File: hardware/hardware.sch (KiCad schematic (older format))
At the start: 76 parts, among them J1 DB25_Female, J2 USB_B_Micro, J3 RJ45_Bel_SI-60062-F-68net, J4 Conn_02x06_Odd_Even, U1 LD1117S33TR_SOT223, U11 ENC28J60x-SO, U12 74HC14, U2 74LS126, U3 74LS126, U4 LM1117-ADJ, U5 74LS126, U6 74LS126, U7 STM32F072R8Tx, U8 74LS245, Y1 8MHz, Y2 25MHz

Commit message: feat: split 15 resistor array into single resistors
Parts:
- removed R8: resistor_array_15, Package_SO:SOIC-16_3.9x9.9mm_P1.27mm, symbol 68net:resistor_array_15
- added R21, R22, R23, R24, R25, R26, R27, R28, R29, R30, R31, R32, R33, R34, R8: 3k3, Resistor_SMD:R_0805_2012Metric_Pad1.15x1.40mm_HandSolder, symbol Device:R
- J4: footprint Connector_PinHeader_1.27mm:PinHeader_2x06_P1.27mm_Vertical -> Connector_PinSocket_2.54mm:PinSocket_2x06_P2.54mm_Vertical
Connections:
- wire segments 531 -> 559
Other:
- note added: "Extension port"
- note removed: "Expansion port"
- moved on the sheet: U2A, U2B, U2C, U2D, U3A, U3C, U3D, U5A, U5B, U5C, U5D, U6A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

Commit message: feat: finalize revA-alpha
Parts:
- removed J4: Conn_02x06_Odd_Even, Connector_PinSocket_2.54mm:PinSocket_2x06_P2.54mm_Vertical, symbol Connector_Generic:Conn_02x06_Odd_Even
- removed JP1: SJ, Jumper:SolderJumper-2_P1.3mm_Bridged_RoundedPad1.0x1.5mm, symbol Jumper:SolderJumper_2_Bridged
- removed JP2: SJ, Jumper:SolderJumper-2_P1.3mm_Open_RoundedPad1.0x1.5mm, symbol Jumper:SolderJumper_2_Open
- removed R11: 22, Resistor_SMD:R_0805_2012Metric_Pad1.15x1.40mm_HandSolder, symbol Device:R
- added C25: 100uF, Capacitor_SMD:CP_Elec_6.3x5.4, symbol Device:C
- added C28, C34, C35: 100nF, Capacitor_SMD:C_1206_3216Metric_Pad1.42x1.75mm_HandSolder, symbol Device:C
- added D3, D4: D_Schottky, Diode_SMD:D_SOD-523, symbol Device:D_Schottky
- added H1, H2, H3, H4: MountingHole, MountingHole:MountingHole_3.2mm_M3_Pad, symbol Mechanical:MountingHole
- R4: value 330 -> 165; Digi-Key_PN RMCF0805JT330RCT-ND -> RMCF0805FT165RCT-ND
- U1: value LD1117S33TR_SOT223 -> LD1117 3.3
- U12: value 74HC14 -> 74LVC14
- U2, U3, U5, U6: value 74LS126 -> 74LVTH126
- U8: value 74LS245 -> 74LVC245; Digi-Key_PN (none) -> 296-1232-1-ND
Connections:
- net labels added: TPWR, VCC
- net labels removed: GPIO_0, GPIO_1, GPIO_2, GPIO_3, UART_RX, UART_TX
- no-connect marks 14 -> 21
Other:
- note added: "VCC: voltage around 4/5V from SCSI and USB\nVBUS: 2.85V generated on-board\n5V: 5V from USB\n3V3: 3.3V generated on-board\n"
- note added: "Voltages:"
- note removed: "Extension port"
- moved on the sheet: C23, C24, C26, C27, FB1, J3, R13, R17, R18, R19, R20

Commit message: feat: add jumper connector to enable termination
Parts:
- added JP1: Jumper_2_Bridged, Connector_PinHeader_2.54mm:PinHeader_1x02_P2.54mm_Vertical, symbol Jumper:Jumper_2_Bridged
- S1, S2: Digi-Key_PN 486-3465-ND -> TL3301AF160QG
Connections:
- net VBUS: now also JP1.2 (B); no longer C3.1, C4.1, RN1.1 (common), RN2.1 (common)
- new net: C3.1, C4.1, JP1.1 (A), RN1.1 (common), RN2.1 (common)
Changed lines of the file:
@@
 DBP
 Wire Wire Line
-	12200 5600 12050 5600
-Wire Wire Line
 	12050 5600 12050 5500
 Wire Wire Line
@@
 F 2 "digikey-footprints:Switch_Tactile_SMD_6x6mm" H 1550 1000 60  0001 L CNN
 F 3 "https://www.ckswitches.com/media/1471/pts645.pdf" H 1550 1100 60  0001 L CNN
-F 4 "486-3465-ND" H 1550 1200 60  0001 L CNN "Digi-Key_PN"
+F 4 "TL3301AF160QG" H 1550 1200 60  0001 L CNN "Digi-Key_PN"
 F 5 "" H 1550 1300 60  0001 L CNN "MPN"
 F 6 "Switches" H 1550 1400 60  0001 L CNN "Category"
@@
 F 2 "digikey-footprints:Switch_Tactile_SMD_6x6mm" H 1550 2000 60  0001 L CNN
 F 3 "https://www.ckswitches.com/media/1471/pts645.pdf" H 1550 2100 60  0001 L CNN
-F 4 "486-3465-ND" H 1550 2200 60  0001 L CNN "Digi-Key_PN"
+F 4 "TL3301AF160QG" H 1550 2200 60  0001 L CNN "Digi-Key_PN"
 F 5 "" H 1550 2300 60  0001 L CNN "MPN"
 F 6 "Switches" H 1550 2400 60  0001 L CNN "Category"
@@
 	3350 10250 3500 10250
 Wire Wire Line
-	3500 10250 3500 10700
+	3500 10250 3500 10550
 Connection ~ 3500 10250
 Wire Wire Line
@@
 	1    0    0    -1
 $EndComp
-Wire Wire Line
-	15150 5400 15150 5300
 Connection ~ 15150 5400
-Wire Wire Line
-	15150 4150 15150 4050
 Connection ~ 15150 4150
 $Comp
 L power:VBUS #PWR?
-U 1 1 60657233
-P 15150 5300
-F 0 "#PWR?" H 15150 5150 50  0001 C CNN
-F 1 "VBUS" H 15165 5473 50  0000 C CNN
-F 2 "" H 15150 5300 50  0001 C CNN
-F 3 "" H 15150 5300 50  0001 C CNN
-	1    15150 5300
-	1    0    0    -1
-$EndComp
-$Comp
-L power:VBUS #PWR?
 U 1 1 60658E91
-P 15150 4050
-F 0 "#PWR?" H 15150 3900 50  0001 C CNN
-F 1 "VBUS" H 15165 4223 50  0000 C CNN
-F 2 "" H 15150 4050 50  0001 C CNN
-F 3 "" H 15150 4050 50  0001 C CNN
-	1    15150 4050
+P 15800 3800
+F 0 "#PWR?" H 15800 3650 50  0001 C CNN
+F 1 "VBUS" H 15815 3973 50  0000 C CNN
+F 2 "" H 15800 3800 50  0001 C CNN
+F 3 "" H 15800 3800 50  0001 C CNN
+	1    15800 3800
 	1    0    0    -1
 $EndComp
@@
 NoConn ~ 3700 5800
 NoConn ~ -2550 -1750
+$Comp
+L Jumper:Jumper_2_Bridged JP1
+U 1 1 5FB8237D
+P 15500 3900
+F 0 "JP1" H 15500 4095 50  0000 C CNN
+F 1 "Jumper_2_Bridged" H 15500 4004 50  0000 C CNN
+F 2 "Connector_PinHeader_2.54mm:PinHeader_1x02_P2.54mm_Vertical" H 15500 3900 50  0001 C CNN
+F 3 "~" H 15500 3900 50  0001 C CNN
+	1    15500 3900
+	1    0    0    -1
+$EndComp
+Wire Wire Line
+	15800 3800 15800 3900
+Wire Wire Line
+	15800 3900 15700 3900
+Wire Wire Line
+	15300 3900 15250 3900
+Wire Wire Line
+	15150 3900 15150 4150
+Wire Wire Line
+	15250 3900 15250 4250
+Wire Wire Line
+	15250 4250 15450 4250
+Wire Wire Line
+	15450 4250 15450 5400
+Wire Wire Line
+	15450 5400 15150 5400
+Connection ~ 15250 3900
+Wire Wire Line
+	15250 3900 15150 3900
+Wire Wire Line
+	12200 5600 12050 5600
+$Comp
+L power:PWR_FLAG #FLG?
+U 1 1 603067E4
+P 3500 10550
+F 0 "#FLG?" H 3500 10625 50  0001 C CNN
+F 1 "PWR_FLAG" V 3500 10677 50  0000 L CNN
+F 2 "" H 3500 10550 50  0001 C CNN
+F 3 "~" H 3500 10550 50  0001 C CNN
+	1    3500 10550
+	0    -1   -1   0
+$EndComp
+Connection ~ 3500 10550
+Wire Wire Line
+	3500 10550 3500 10700
 $EndSCHEMATC

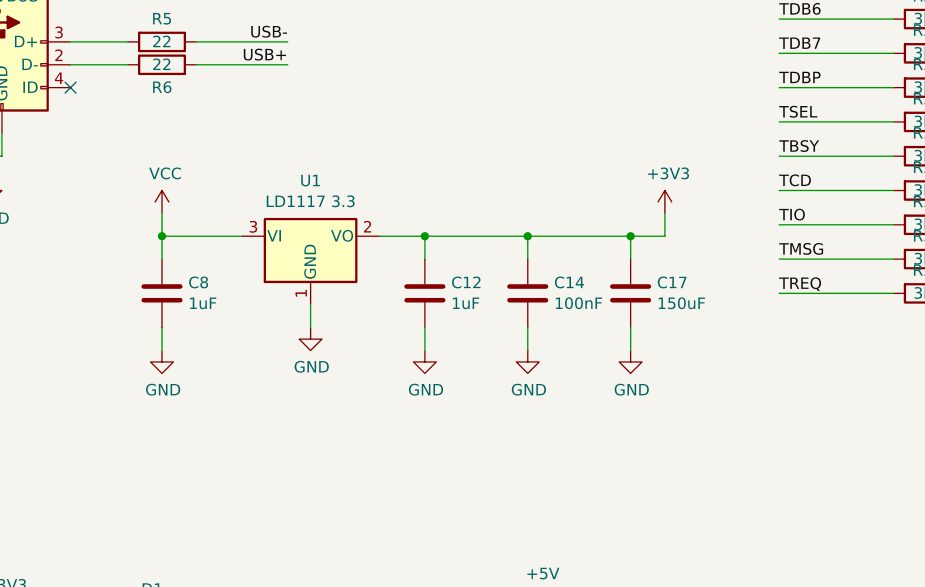
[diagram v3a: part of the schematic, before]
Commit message: feat: update LDO regulator
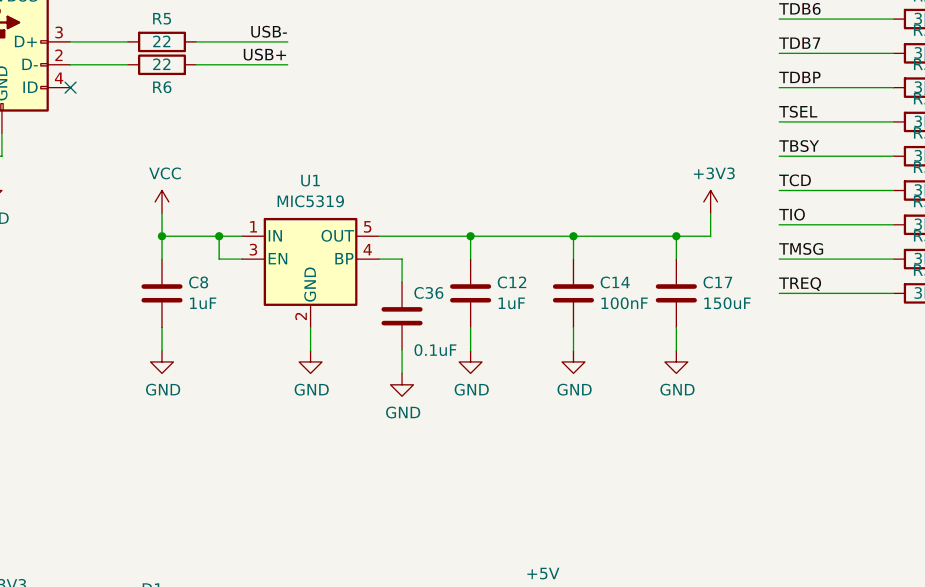
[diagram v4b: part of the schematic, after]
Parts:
- removed U1: LD1117 3.3, Package_TO_SOT_SMD:SOT-223-3_TabPin2, symbol Regulator_Linear:LD1117S33TR_SOT223
- added C36: 0.1uF, Capacitor_SMD:C_1206_3216Metric_Pad1.42x1.75mm_HandSolder, symbol Device:C
- added U1: MIC5319, Package_TO_SOT_SMD:SOT-23-5_HandSoldering, symbol Regulator_Linear:LDK130-08_SOT23_SOT353
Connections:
- net +3V3: now also U1.5 (OUT)
- net GND: now also C36.2, U1.2 (GND)
- net VCC: now also U1.1 (IN), U1.3 (EN)
- new net: C36.1, U1.4 (BP)
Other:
- moved on the sheet: C12, C14, C17
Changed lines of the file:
@@
 NoConn ~ 12300 8400
 Wire Wire Line
-	2350 8400 2350 8500
+	2350 8500 2350 8600
 $Comp
 L power:GND #PWR?
 U 1 1 603F21C0
-P 2350 8500
-F 0 "#PWR?" H 2350 8250 50  0001 C CNN
-F 1 "GND" H 2355 8327 50  0000 C CNN
-F 2 "" H 2350 8500 50  0001 C CNN
-F 3 "" H 2350 8500 50  0001 C CNN
-	1    2350 8500
-	1    0    0    -1
-$EndComp
-Wire Wire Line
-	2050 8100 1700 8100
+P 2350 8600
+F 0 "#PWR?" H 2350 8350 50  0001 C CNN
+F 1 "GND" H 2355 8427 50  0000 C CNN
+F 2 "" H 2350 8600 50  0001 C CNN
+F 3 "" H 2350 8600 50  0001 C CNN
+	1    2350 8600
+	1    0    0    -1
+$EndComp
+Wire Wire Line
+	2050 8100 1950 8100
 Wire Wire Line
 	1700 8100 1700 8000
@@
 $EndComp
 Wire Wire Line
-	2650 8100 2850 8100
-Wire Wire Line
-	2850 8100 2850 8200
-Connection ~ 2850 8100
-Wire Wire Line
-	2850 8100 3300 8100
-Wire Wire Line
-	3300 8100 3300 8200
-Connection ~ 3300 8100
-Wire Wire Line
-	3750 8100 3750 8200
-Wire Wire Line
-	3300 8100 3750 8100
-Wire Wire Line
-	3750 8100 3900 8100
-Wire Wire Line
-	3900 8100 3900 8000
-Connection ~ 3750 8100
+	3050 8100 3050 8200
+Connection ~ 3050 8100
+Wire Wire Line
+	3050 8100 3500 8100
+Wire Wire Line
+	3500 8100 3500 8200
+Connection ~ 3500 8100
+Wire Wire Line
+	3950 8100 3950 8200
+Wire Wire Line
+	3500 8100 3950 8100
+Wire Wire Line
+	3950 8100 4100 8100
+Wire Wire Line
+	4100 8100 4100 8000
+Connection ~ 3950 8100
 $Comp
 L power:+3V3 #PWR?
 U 1 1 604FDB0C
-P 3900 8000
-F 0 "#PWR?" H 3900 7850 50  0001 C CNN
-F 1 "+3V3" H 3915 8173 50  0000 C CNN
-F 2 "" H 3900 8000 50  0001 C CNN
-F 3 "" H 3900 8000 50  0001 C CNN
-	1    3900 8000
-	1    0    0    -1
-$EndComp
-Wire Wire Line
-	2850 8500 2850 8600
-Wire Wire Line
-	3300 8500 3300 8600
-Wire Wire Line
-	3750 8500 3750 8600
+P 4100 8000
+F 0 "#PWR?" H 4100 7850 50  0001 C CNN
+F 1 "+3V3" H 4115 8173 50  0000 C CNN
+F 2 "" H 4100 8000 50  0001 C CNN
+F 3 "" H 4100 8000 50  0001 C CNN
+	1    4100 8000
+	1    0    0    -1
+$EndComp
+Wire Wire Line
+	3050 8500 3050 8600
+Wire Wire Line
+	3500 8500 3500 8600
+Wire Wire Line
+	3950 8500 3950 8600
 $Comp
 L power:GND #PWR?
 U 1 1 60564AE3
-P 2850 8600
-F 0 "#PWR?" H 2850 8350 50  0001 C CNN
-F 1 "GND" H 2855 8427 50  0000 C CNN
-F 2 "" H 2850 8600 50  0001 C CNN
-F 3 "" H 2850 8600 50  0001 C CNN
-	1    2850 8600
+P 3050 8600
+F 0 "#PWR?" H 3050 8350 50  0001 C CNN
+F 1 "GND" H 3055 8427 50  0000 C CNN
+F 2 "" H 3050 8600 50  0001 C CNN
+F 3 "" H 3050 8600 50  0001 C CNN
+	1    3050 8600
 	1    0    0    -1
 $EndComp
@@
 L power:GND #PWR?
 U 1 1 60565F7F
-P 3300 8600
-F 0 "#PWR?" H 3300 8350 50  0001 C CNN
-F 1 "GND" H 3305 8427 50  0000 C CNN
-F 2 "" H 3300 8600 50  0001 C CNN
-F 3 "" H 3300 8600 50  0001 C CNN
-	1    3300 8600
+P 3500 8600
+F 0 "#PWR?" H 3500 8350 50  0001 C CNN
+F 1 "GND" H 3505 8427 50  0000 C CNN
+F 2 "" H 3500 8600 50  0001 C CNN
+F 3 "" H 3500 8600 50  0001 C CNN
+	1    3500 8600
 	1    0    0    -1
 $EndComp
@@
 L power:GND #PWR?
 U 1 1 6056735B
-P 3750 8600
-F 0 "#PWR?" H 3750 8350 50  0001 C CNN
-F 1 "GND" H 3755 8427 50  0000 C CNN
-F 2 "" H 3750 8600 50  0001 C CNN
-F 3 "" H 3750 8600 50  0001 C CNN
-	1    3750 8600
+P 3950 8600
+F 0 "#PWR?" H 3950 8350 50  0001 C CNN
+F 1 "GND" H 3955 8427 50  0000 C CNN
+F 2 "" H 3950 8600 50  0001 C CNN
+F 3 "" H 3950 8600 50  0001 C CNN
+	1    3950 8600
 	1    0    0    -1
 $EndComp
@@
 L Device:C C17
 U 1 1 604B9132
-P 3750 8350
-F 0 "C17" H 3865 8396 50  0000 L CNN
-F 1 "150uF" H 3865 8305 50  0000 L CNN
-F 2 "Capacitor_SMD:C_1206_3216Metric_Pad1.42x1.75mm_HandSolder" H 3788 8200 50  0001 C CNN
-F 3 "~" H 3750 8350 50  0001 C CNN
-F 4 "490-13964-1-ND" H 3750 8350 50  0001 C CNN "Digi-Key_PN"
-	1    3750 8350
+P 3950 8350
+F 0 "C17" H 4065 8396 50  0000 L CNN
+F 1 "150uF" H 4065 8305 50  0000 L CNN
+F 2 "Capacitor_SMD:C_1206_3216Metric_Pad1.42x1.75mm_HandSolder" H 3988 8200 50  0001 C CNN
+F 3 "~" H 3950 8350 50  0001 C CNN
+F 4 "490-13964-1-ND" H 3950 8350 50  0001 C CNN "Digi-Key_PN"
+	1    3950 8350
 	1    0    0    -1
 $EndComp
@@
 L Device:C C14
 U 1 1 604B7CD6
-P 3300 8350
-F 0 "C14" H 3415 8396 50  0000 L CNN
-F 1 "100nF" H 3415 8305 50  0000 L CNN
-F 2 "Capacitor_SMD:C_1206_3216Metric_Pad1.42x1.75mm_HandSolder" H 3338 8200 50  0001 C CNN
-F 3 "~" H 3300 8350 50  0001 C CNN
-F 4 "1276-1017-1-ND" H 3300 8350 50  0001 C CNN "Digi-Key_PN"
-	1    3300 8350
+P 3500 8350
+F 0 "C14" H 3615 8396 50  0000 L CNN
+F 1 "100nF" H 3615 8305 50  0000 L CNN
+F 2 "Capacitor_SMD:C_1206_3216Metric_Pad1.42x1.75mm_HandSolder" H 3538 8200 50  0001 C CNN
+F 3 "~" H 3500 8350 50  0001 C CNN
+F 4 "1276-1017-1-ND" H 3500 8350 50  0001 C CNN "Digi-Key_PN"
+	1    3500 8350
 	1    0    0    -1
 $EndComp
@@
 L Device:C C12
 U 1 1 60495FA0
-P 2850 8350
-F 0 "C12" H 2965 8396 50  0000 L CNN
-F 1 "1uF" H 2965 8305 50  0000 L CNN
-F 2 "Capacitor_SMD:C_1206_3216Metric_Pad1.42x1.75mm_HandSolder" H 2888 8200 50  0001 C CNN
-F 3 "~" H 2850 8350 50  0001 C CNN
-F 4 "1276-3091-1-ND" H 2850 8350 50  0001 C CNN "Digi-Key_PN"
-	1    2850 8350
+P 3050 8350
+F 0 "C12" H 3165 8396 50  0000 L CNN
+F 1 "1uF" H 3165 8305 50  0000 L CNN
+F 2 "Capacitor_SMD:C_1206_3216Metric_Pad1.42x1.75mm_HandSolder" H 3088 8200 50  0001 C CNN
+F 3 "~" H 3050 8350 50  0001 C CNN
+F 4 "1276-3091-1-ND" H 3050 8350 50  0001 C CNN "Digi-Key_PN"
+	1    3050 8350
 	1    0    0    -1
 $EndComp
@@
 F 4 "609-1507-ND" H 15250 2050 50  0001 C CNN "Digi-Key_PN"
 	1    15250 2050
-	1    0    0    -1
-$EndComp
-$Comp
-L Regulator_Linear:LD1117S33TR_SOT223 U1
-U 1 1 603D199E
-P 2350 8100
-F 0 "U1" H 2350 8342 50  0000 C CNN
-F 1 "LD1117 3.3" H 2350 8251 50  0000 C CNN
-F 2 "Package_TO_SOT_SMD:SOT-223-3_TabPin2" H 2350 8300 50  0001 C CNN
-F 3 "http://www.st.com/st-web-ui/static/active/en/resource/technical/document/datasheet/CD00000544.pdf" H 2450 7850 50  0001 C CNN
-F 4 "497-1242-1-ND" H 2350 8100 50  0001 C CNN "Digi-Key_PN"
-	1    2350 8100
 	1    0    0    -1
 $EndComp
@@
 Wire Wire Line
 	3500 10550 3500 10700
+Wire Wire Line
+	1950 8100 1950 8200
+Wire Wire Line
+	1950 8200 2050 8200
+Connection ~ 1950 8100
+Wire Wire Line
+	1950 8100 1700 8100
+Wire Wire Line
+	2650 8100 3050 8100
+Wire Wire Line
+	2750 8600 2750 8700
+$Comp
+L power:GND #PWR?
+U 1 1 60531898
+P 2750 8700
+F 0 "#PWR?" H 2750 8450 50  0001 C CNN
+F 1 "GND" H 2755 8527 50  0000 C CNN
+F 2 "" H 2750 8700 50  0001 C CNN
+F 3 "" H 2750 8700 50  0001 C CNN
+	1    2750 8700
+	1    0    0    -1
+$EndComp
+$Comp
+L Device:C C36
+U 1 1 6053189F
+P 2750 8450
+F 0 "C36" H 2800 8550 50  0000 L CNN
+F 1 "0.1uF" H 2800 8300 50  0000 L CNN
+F 2 "Capacitor_SMD:C_1206_3216Metric_Pad1.42x1.75mm_HandSolder" H 2788 8300 50  0001 C CNN
+F 3 "~" H 2750 8450 50  0001 C CNN
+F 4 "CL31B104KBCNNNC" H 2750 8450 50  0001 C CNN "Digi-Key_PN"
+	1    2750 8450
+	1    0    0    -1
+$EndComp
+Wire Wire Line
+	2650 8200 2750 8200
+Wire Wire Line
+	2750 8200 2750 8300
+$Comp
+L Regulator_Linear:LDK130-08_SOT23_SOT353 U1
+U 1 1 6065B4B5
+P 2350 8200
+F 0 "U1" H 2350 8542 50  0000 C CNN
+F 1 "MIC5319" H 2350 8451 50  0000 C CNN
+F 2 "Package_TO_SOT_SMD:SOT-23-5_HandSoldering" H 2350 8525 50  0001 C CNN
+F 3 "http://www.st.com/content/ccc/resource/technical/document/datasheet/29/10/f7/87/2f/66/47/f4/DM00076097.pdf/files/DM00076097.pdf/jcr:content/translations/en.DM00076097.pdf" H 2350 8200 50  0001 C CNN
+F 4 "MIC5319-3.3YD5-TR" H 2350 8200 50  0001 C CNN "Digi-Key_PN"
+	1    2350 8200
+	1    0    0    -1
+$EndComp
 $EndSCHEMATC
